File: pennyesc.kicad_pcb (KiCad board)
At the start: 4 copper layers, 60 x 19 mm, 48 parts, among them U1 STM32L011F4Ux, U2 MCT8316Z0RRGFR, U3 TMAG5273A1QDBVR

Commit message: finish v1 and order from jlcpcb
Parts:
- removed the C1 at (43.7, 50.1)
- removed the C2 at (44.3, 51.8)
- removed the C3 at (54.2, 55.4)
- removed the C4 at (52.0, 53.1)
- removed the C5 at (51.7, 56.0)
- removed the C6 at (52.2, 45.5)
- removed the C7 at (51.2, 43.8)
- removed the R1 at (52.4, 54.6)
- removed the R2 at (51.6, 47.1)
- removed the R3 at (55.9, 54.3)
- removed the R4 at (55.9, 55.2)
- removed the R5 at (45.0, 46.4)
- removed the R6 at (46.4, 45.0)
- removed the TP1 at (45.1, 47.4)
- removed the TP2 at (56.5, 50.5)
- removed the TP3 at (56.5, 49.4)
- removed the TP4 at (43.8, 51.2)
- removed the TP5 at (43.8, 49.2)
- removed the TP6 at (56.5, 45.5)
- removed the TP7 at (55.4, 44.1)
- removed the TP8 at (53.6, 44.0)
- removed the U1 at (46.5, 53.5)
- removed the U2 at (55.4, 50.0)
- removed the U3 at (47.2, 47.3)
- added TP10: TestPoint, pennyesc:Power_Pad_Rect, B.Cu at (56.1, 47.5)
- added TP11: TestPoint, pennyesc:TestPoint_Pad_1mm, B.Cu at (47.5, 53.7)
- added TP9: TestPoint, pennyesc:Power_Pad_Rect, B.Cu at (56.1, 52.5)
- TP1: footprint pennyesc:TestPoint_Pad_Rect -> pennyesc:TestPoint_Pad_1mm
- moved R1 21.7 mm to (52.6, 45.2), turned to 0 degrees
- moved R2 20.8 mm to (56.0, 45.0), turned to 90 degrees
- moved C5 20.5 mm to (51.6, 52.8)
- moved C4 20.5 mm to (51.6, 46.9), turned to -90 degrees
- moved R3 20.4 mm to (55.0, 45.0)
- moved C1 20.4 mm to (43.7, 50.1)
- moved R4 20.4 mm to (54.5, 43.6)
- moved TP8 20.4 mm to (56.3, 54.7)
- moved U1 20.4 mm to (46.5, 46.5)
- moved TP6 20.4 mm to (53.1, 55.9)
- moved R6 20.4 mm to (45.0, 53.6)
- moved U2 20.4 mm to (55.5, 50.0)
- moved U3 20.3 mm to (47.2, 52.8)
- moved R5 20.3 mm to (46.4, 55.0), turned to -45 degrees
- moved TP7 20.3 mm to (54.9, 55.8)
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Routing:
- net +3.3V: track 0.83 -> 24.9 mm, vias 2 -> 7
- net /UART_TX: track 0.00 -> 18.0 mm, vias 0 -> 1
- net /UART_RX: track 0.00 -> 16.2 mm, vias 0 -> 1
- net /SPI_MOSI: track 0.00 -> 14.4 mm, vias 0 -> 2
- net /SWCLK: track 0.00 -> 14.1 mm, vias 0 -> 1
- net /SWDIO: track 0.00 -> 13.1 mm, vias 0 -> 1
- net /SPI_MISO: track 0.00 -> 13.1 mm, vias 0 -> 2
- net /HALLB: track 0.00 -> 13.1 mm, vias 0 -> 2
- net /HALLA: track 1.10 -> 14.0 mm
- net GND: track 3.41 -> 14.9 mm, vias 0 -> 19
- net /HALLC: track 0.00 -> 11.0 mm, vias 0 -> 2
- net /SPI_SCLK: track 0.00 -> 10.6 mm, vias 0 -> 2
- net /I2C_SCL: track 0.00 -> 10.5 mm, vias 0 -> 2
- net /PWM: track 0.00 -> 10.0 mm, vias 0 -> 2
- net /SPI_CS: track 0.00 -> 9.75 mm, vias 0 -> 2
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- added copper zone on In1.Cu, net +3.3V
- added copper zone on F.Cu, net /OUTA
- added copper zone on F.Cu, net /OUTB
- added copper zone on F.Cu, net /OUTC
- added copper zone on B.Cu, net GND
- added copper zone on F.Cu, net GND
- added copper zone on In2.Cu, net GND
- added copper zone on B.Cu, net VBUS
- added copper zone on F.Cu, net VBUS
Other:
- board size 60 x 19 mm -> 15.9 x 14 mm
- board text added: "4.5-35"
- board text added: "GND"
- board text added: "RX"
- board text added: "TX"
- board text added: "V+"
- board text added: "gnd"
- board text added: "nrst"
- board text added: "pennyesc"
- board text added: "swclk"
- board text added: "swio"
- board text added: "v1"
- board text removed: "penny for scale"

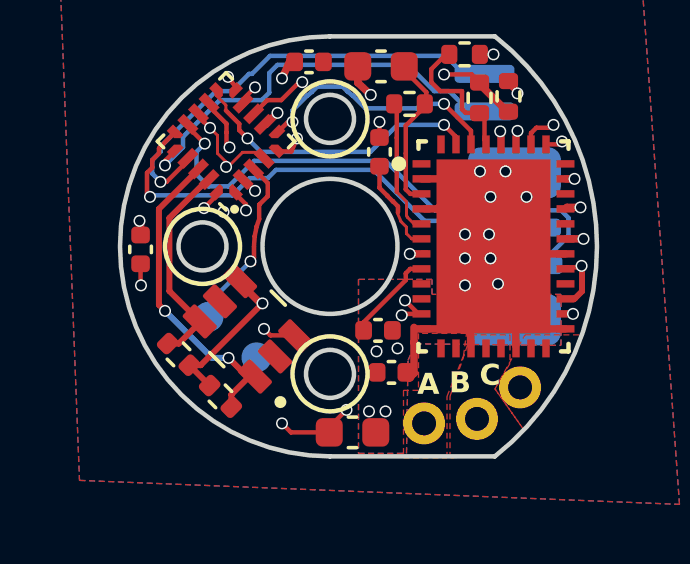
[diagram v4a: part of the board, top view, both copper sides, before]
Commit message: octant LUT for off axis magnetic encoder, staircase artifacts left
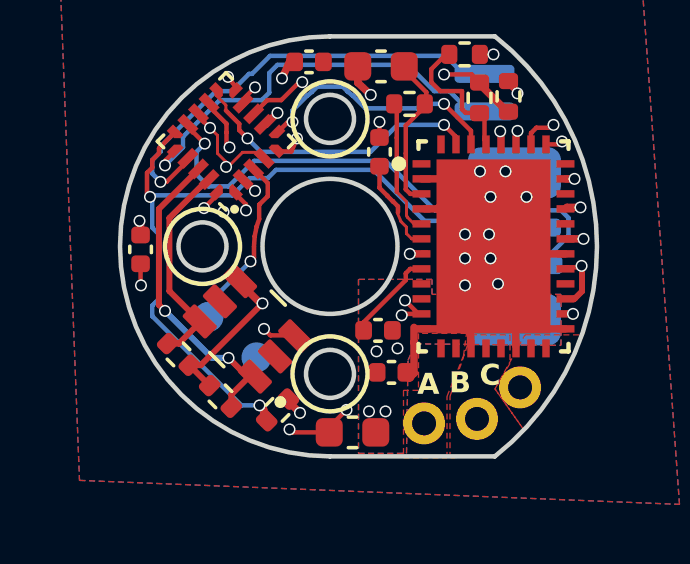
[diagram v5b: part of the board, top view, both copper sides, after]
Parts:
- added R8: 3.3k, Resistor_SMD:R_0402_1005Metric, F.Cu at (48.2, 55.5)
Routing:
- net /UART_RX: track 16.2 -> 25.9 mm, vias 1 -> 2
- net +3.3V: track 24.9 -> 25.5 mm, vias 7 -> 8
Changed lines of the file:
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@@
+  )
+  (footprint "Resistor_SMD:R_0402_1005Metric" (layer "F.Cu")
+    (at 48.25 55.45 -135)
+    (descr "Resistor SMD 0402 (1005 Metric), square (rectangular) end terminal, IPC_7351 nominal, (Body size source: IPC-SM-782 page 72, https://www.pcb-3d.com/wordpress/wp-content/uploads/ipc-sm-782a_amendment_1_and_2.pdf), generated with kicad-footprint-generator")
+    (tags "resistor")
+    (property "FT Rotation Offset" "")
+    (property "JLCPCB" "C25890")
+    (property "LCSC PN" "C25890")
+    (property "MP" "0402WGF3301TCE")
+    (property "Sheetfile" "pennyesc.kicad_sch")
+    (property "Sheetname" "")
+    (property "ki_description" "Resistor, small US symbol")
+    (property "ki_keywords" "r resistor")
+    (attr smd)
+    (fp_text reference "R8" (at 0 -1.17 45) (layer "F.SilkS") hide
+        (effects (font (size 1 1) (thickness 0.15)))
+    )
+    (fp_text value "3.3k" (at 0 1.17 45) (layer "F.Fab")
+        (effects (font (size 1 1) (thickness 0.15)))
+    )
+    (fp_text user "${REFERENCE}" (at 0 0 45) (layer "F.Fab")
+        (effects (font (size 0.26 0.26) (thickness 0.04)))
+    )
+    (fp_line (start -0.153641 -0.38) (end 0.153641 -0.38)
+      (stroke (width 0.12) (type solid)) (layer "F.SilkS"))
+    (fp_line (start -0.153641 0.38) (end 0.153641 0.38)
+      (stroke (width 0.12) (type solid)) (layer "F.SilkS"))
+    (fp_line (start -0.93 -0.47) (end 0.93 -0.47)
+      (stroke (width 0.05) (type solid)) (layer "F.CrtYd"))
+    (fp_line (start -0.93 0.47) (end -0.93 -0.47)
+      (stroke (width 0.05) (type solid)) (layer "F.CrtYd"))
+    (fp_line (start 0.93 -0.47) (end 0.93 0.47)
+      (stroke (width 0.05) (type solid)) (layer "F.CrtYd"))
+    (fp_line (start 0.93 0.47) (end -0.93 0.47)
+      (stroke (width 0.05) (type solid)) (layer "F.CrtYd"))
+    (fp_line (start -0.525 -0.27) (end 0.525 -0.27)
+      (stroke (width 0.1) (type solid)) (layer "F.Fab"))
+    (fp_line (start -0.525 0.27) (end -0.525 -0.27)
+      (stroke (width 0.1) (type solid)) (layer "F.Fab"))
+    (fp_line (start 0.525 -0.27) (end 0.525 0.27)
+      (stroke (width 0.1) (type solid)) (layer "F.Fab"))
+    (fp_line (start 0.525 0.27) (end -0.525 0.27)
+      (stroke (width 0.1) (type solid)) (layer "F.Fab"))
+    (pad "1" smd roundrect (at -0.51 0 225) (size 0.54 0.64) (layers "F.Cu" "F.Paste" "F.Mask") (roundrect_rratio 0.25)
+      (net 2 "+3.3V") (pintype "passive"))
+    (pad "2" smd roundrect (at 0.51 0 225) (size 0.54 0.64) (layers "F.Cu" "F.Paste" "F.Mask") (roundrect_rratio 0.25)
+      (net 9 "/UART_RX") (pintype "passive"))
+    (model "${KICAD6_3DMODEL_DIR}/Resistor_SMD.3dshapes/R_0402_1005Metric.wrl"
+      (offset (xyz 0 0 0))
+      (scale (xyz 1 1 1))
+      (rotate (xyz 0 0 0))
+    )
   )
   (footprint "Resistor_SMD:R_0402_1005Metric" (layer "F.Cu")
@@
   (segment (start 49.975 56.025) (end 50.55 55.45) (width 0.15) (layer "F.Cu") (net 1))
   (segment (start 53.572764 48.75) (end 53.722675 48.600089) (width 0.25) (layer "F.Cu") (net 1))
+  (segment (start 48.65 56.1) (end 48.75 56.2) (width 0.15) (layer "F.Cu") (net 1))
   (segment (start 46.55 46.6) (end 46.65 46.7) (width 0.15) (layer "F.Cu") (net 1))
   (segment (start 48.80917 52.965668) (end 48.015668 52.965668) (width 0.15) (layer "F.Cu") (net 1))
   (segment (start 52.8 53.2) (end 52.8 52.7) (width 0.25) (layer "F.Cu") (net 1))
   (segment (start 46.55 45.913172) (end 46.55 46.2) (width 0.15) (layer "F.Cu") (net 1))
+  (segment (start 48.75 56.2) (end 49.975 56.2) (width 0.15) (layer "F.Cu") (net 1))
   (segment (start 53.15 48.75) (end 53.572764 48.75) (width 0.25) (layer "F.Cu") (net 1))
   (segment (start 56.185876 53.300089) (end 56.185876 52.61329) (width 0.25) (layer "F.Cu") (net 1))
@@
   (segment (start 53.05 52.75) (end 53.75 52.75) (width 0.25) (layer "F.Cu") (net 1))
   (segment (start 46.55 46.2) (end 46.55 46.6) (width 0.15) (layer "F.Cu") (net 1))
-  (segment (start 49.975 56.2) (end 48.7 56.2) (width 0.15) (layer "F.Cu") (net 1))
   (segment (start 55.499589 43.600089) (end 54.995876 43.600089) (width 0.15) (layer "F.Cu") (net 1))
-  (segment (start 48.7 56.2) (end 48.4 55.9) (width 0.15) (layer "F.Cu") (net 1))
   (segment (start 54.685876 53.300089) (end 54.685876 52.636888) (width 0.25) (layer "F.Cu") (net 1))
   (via (at 54.5 51.3) (size 0.4) (drill 0.3) (layers "F.Cu" "B.Cu") (net 1))
@@
   (via (at 55.85 47.5) (size 0.4) (drill 0.3) (layers "F.Cu" "B.Cu") (net 1))
   (via (at 55 47.5) (size 0.4) (drill 0.3) (layers "F.Cu" "B.Cu") (net 1))
-  (via (at 48.4 55.9) (size 0.4) (drill 0.3) (layers "F.Cu" "B.Cu") (net 1))
+  (via (at 48.65 56.1) (size 0.4) (drill 0.3) (layers "F.Cu" "B.Cu") (net 1))
   (via (at 51.357816 44.95) (size 0.4) (drill 0.3) (layers "F.Cu" "B.Cu") (net 1))
   (via (at 54.5 49.6) (size 0.4) (drill 0.3) (layers "F.Cu" "B.Cu") (net 1))
@@
   (segment (start 43.685876 51.185376) (end 43.685876 50.580089) (width 0.15) (layer "F.Cu") (net 2))
   (segment (start 46.535876 47.185876) (end 46.25 46.9) (width 0.1) (layer "F.Cu") (net 2))
+  (segment (start 48.639376 55.189376) (end 49 55.55) (width 0.25) (layer "F.Cu") (net 2))
   (segment (start 45.616637 45.58085) (end 45.616637 45.666637) (width 0.15) (layer "F.Cu") (net 2))
   (segment (start 48.4 44.4) (end 48.65 43.85) (width 0.25) (layer "F.Cu") (net 2))
@@
   (segment (start 57.885876 50.700089) (end 58.335876 50.700089) (width 0.15) (layer "F.Cu") (net 2))
   (segment (start 54.719589 44.269589) (end 54.95 44.5) (width 0.15) (layer "F.Cu") (net 2))
+  (segment (start 48.510624 55.189376) (end 48.639376 55.189376) (width 0.25) (layer "F.Cu") (net 2))
   (segment (start 45.310624 53.960624) (end 45.95 54.6) (width 0.2) (layer "F.Cu") (net 2))
   (segment (start 46.25 46.3) (end 46 46.05) (width 0.1) (layer "F.Cu") (net 2))
@@
   (via (at 43.7 51.3) (size 0.4) (drill 0.3) (layers "F.Cu" "B.Cu") (net 2))
   (via (at 48.4 44.4) (size 0.4) (drill 0.3) (layers "F.Cu" "B.Cu") (net 2))
+  (via (at 49 55.55) (size 0.4) (drill 0.3) (layers "F.Cu" "B.Cu") (net 2))
   (via (at 46 46.05) (size 0.4) (drill 0.3) (layers "F.Cu" "B.Cu") (net 2))
   (via (at 47.75 51.9) (size 0.4) (drill 0.3) (layers "F.Cu" "B.Cu") (net 2))
@@
   (segment (start 44.3 46.898959) (end 44.075 47.123959) (width 0.15) (layer "F.Cu") (net 9))
   (segment (start 44.075 47.375) (end 43.9 47.55) (width 0.15) (layer "F.Cu") (net 9))
+  (segment (start 47.789376 55.439376) (end 47.65 55.3) (width 0.25) (layer "F.Cu") (net 9))
   (segment (start 43.9 47.55) (end 43.9 48.25) (width 0.15) (layer "F.Cu") (net 9))
   (segment (start 44.075 47.123959) (end 44.075 47.375) (width 0.15) (layer "F.Cu") (net 9))
+  (segment (start 47.789376 55.910624) (end 47.789376 55.439376) (width 0.25) (layer "F.Cu") (net 9))
   (segment (start 44.785787 46.164213) (end 44.785787 46.244788) (width 0.15) (layer "F.Cu") (net 9))
+  (via (at 47.65 55.3) (size 0.4) (drill 0.3) (layers "F.Cu" "B.Cu") (net 9))
   (via (at 44 48.35) (size 0.4) (drill 0.3) (layers "F.Cu" "B.Cu") (net 9))
+  (segment (start 47.048959 55.3) (end 47.65 55.3) (width 0.15) (layer "B.Cu") (net 9))
   (segment (start 51.45 47.45) (end 48.199569 47.45) (width 0.15) (layer "B.Cu") (net 9))
+  (segment (start 44.323959 51.725) (end 44.075 51.973959) (width 0.15) (layer "B.Cu") (net 9))
+  (segment (start 44.075 48.425) (end 44.075 49.375) (width 0.15) (layer "B.Cu") (net 9))
+  (segment (start 44.075 52.326041) (end 47.048959 55.3) (width 0.15) (layer "B.Cu") (net 9))
   (segment (start 44.05 48.3) (end 44 48.35) (width 0.15) (layer "B.Cu") (net 9))
   (segment (start 47.323959 47.725) (end 46.748959 48.3) (width 0.15) (layer "B.Cu") (net 9))
   (segment (start 47.924569 47.725) (end 47.323959 47.725) (width 0.15) (layer "B.Cu") (net 9))
   (segment (start 46.748959 48.3) (end 44.05 48.3) (width 0.15) (layer "B.Cu") (net 9))
+  (segment (start 44 48.35) (end 44.075 48.425) (width 0.15) (layer "B.Cu") (net 9))
+  (segment (start 44.323959 49.623959) (end 44.323959 51.725) (width 0.15) (layer "B.Cu") (net 9))
   (segment (start 56.485876 49.350089) (end 56.149911 49.350089) (width 0.15) (layer "B.Cu") (net 9))
   (segment (start 56.149911 49.350089) (end 55.949822 49.15) (width 0.15) (layer "B.Cu") (net 9))
   (segment (start 48.199569 47.45) (end 47.924569 47.725) (width 0.15) (layer "B.Cu") (net 9))
+  (segment (start 44.075 51.973959) (end 44.075 52.326041) (width 0.15) (layer "B.Cu") (net 9))
   (segment (start 55.949822 49.15) (end 53.15 49.15) (width 0.15) (layer "B.Cu") (net 9))
+  (segment (start 44.075 49.375) (end 44.323959 49.623959) (width 0.15) (layer "B.Cu") (net 9))
   (segment (start 53.15 49.15) (end 51.45 47.45) (width 0.15) (layer "B.Cu") (net 9))
   (segment (start 44.5 47.15) (end 44.85 46.8) (width 0.15) (layer "F.Cu") (net 10))

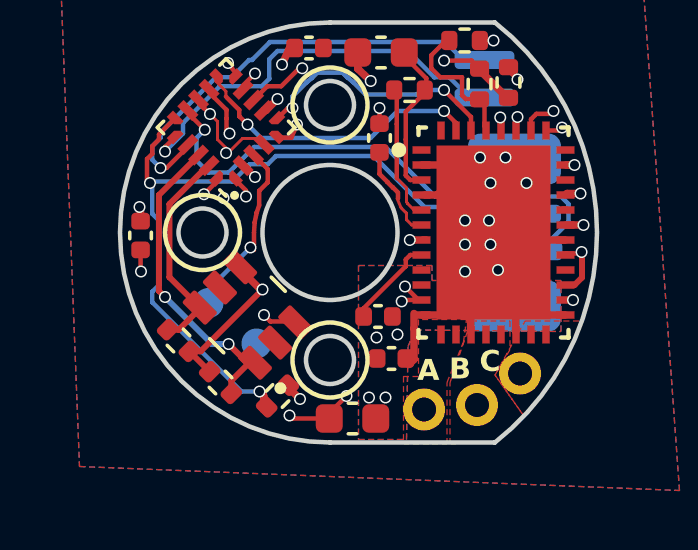
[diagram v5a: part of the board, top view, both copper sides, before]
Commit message: pennyesc pcb v2 ordered
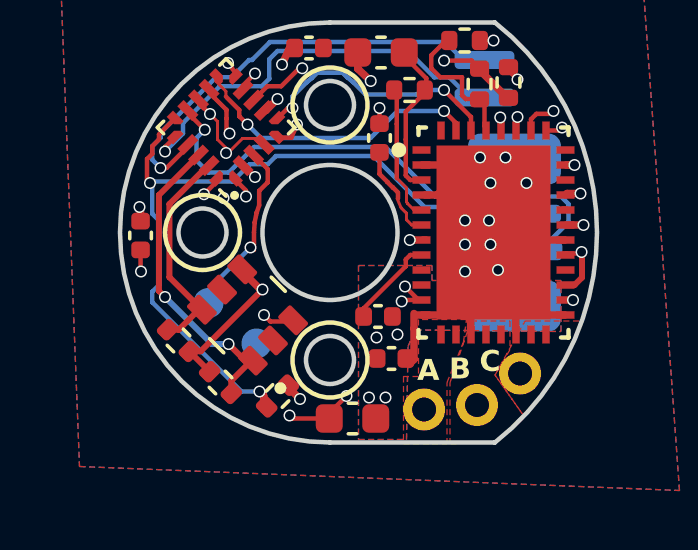
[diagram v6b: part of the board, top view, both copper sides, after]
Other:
- board text added: "v2"
- board text removed: "v1"
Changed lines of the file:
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@@
   (title_block
     (title "PennyESC")
-    (date "2025-10-22")
-    (rev "1")
+    (date "2025-12-25")
+    (rev "2")
     (company "Christopher Xu")
   )
@@
     (fp_circle (center -2.5 -0.95) (end -2.4 -0.95)
       (stroke (width 0.2) (type solid)) (fill none) (layer "F.Fab"))
-    (pad "1" smd roundrect (at -1.3 -0.95 135) (size 1.1 0.6) (layers "F.Cu" "F.Paste" "F.Mask") (roundrect_rratio 0.125)
+    (pad "1" smd roundrect (at -1.2 -0.95 135) (size 0.9 0.6) (layers "F.Cu" "F.Paste" "F.Mask") (roundrect_rratio 0.125)
       (net 20 "/I2C_SCL") (pinfunction "SCL") (pintype "bidirectional"))
-    (pad "2" smd roundrect (at -1.3 0 135) (size 1.1 0.6) (layers "F.Cu" "F.Paste" "F.Mask") (roundrect_rratio 0.125)
+    (pad "2" smd roundrect (at -1.2 0 135) (size 0.9 0.6) (layers "F.Cu" "F.Paste" "F.Mask") (roundrect_rratio 0.125)
       (net 1 "GND") (pinfunction "GND") (pintype "power_in"))
-    (pad "3" smd roundrect (at -1.3 0.95 135) (size 1.1 0.6) (layers "F.Cu" "F.Paste" "F.Mask") (roundrect_rratio 0.125)
+    (pad "3" smd roundrect (at -1.2 0.95 135) (size 0.9 0.6) (layers "F.Cu" "F.Paste" "F.Mask") (roundrect_rratio 0.125)
       (net 1 "GND") (pinfunction "TEST") (pintype "input"))
-    (pad "4" smd roundrect (at 1.3 0.95 135) (size 1.1 0.6) (layers "F.Cu" "F.Paste" "F.Mask") (roundrect_rratio 0.125)
+    (pad "4" smd roundrect (at 1.2 0.95 135) (size 0.9 0.6) (layers "F.Cu" "F.Paste" "F.Mask") (roundrect_rratio 0.125)
       (net 2 "+3.3V") (pinfunction "VCC") (pintype "power_in"))
-    (pad "5" smd roundrect (at 1.3 0 135) (size 1.1 0.6) (layers "F.Cu" "F.Paste" "F.Mask") (roundrect_rratio 0.125)
+    (pad "5" smd roundrect (at 1.2 0 135) (size 0.9 0.6) (layers "F.Cu" "F.Paste" "F.Mask") (roundrect_rratio 0.125)
       (net 36 "unconnected-(U3-~{INT}-Pad5)") (pinfunction "~{INT}") (pintype "bidirectional+no_connect"))
-    (pad "6" smd roundrect (at 1.3 -0.95 135) (size 1.1 0.6) (layers "F.Cu" "F.Paste" "F.Mask") (roundrect_rratio 0.125)
+    (pad "6" smd roundrect (at 1.2 -0.95 135) (size 0.9 0.6) (layers "F.Cu" "F.Paste" "F.Mask") (roundrect_rratio 0.125)
       (net 21 "/I2C_SDA") (pinfunction "SDA") (pintype "bidirectional"))
     (model "${KIPRJMOD}/pennyesc.pretty/TMAG5273A1QDBVR.step"
@@
     (effects (font (size 0.7 0.7) (thickness 0.15)) (justify left bottom mirror))
   )
-  (gr_text "v1" (at 48.35 46.85 45) (layer "B.SilkS")
+  (gr_text "v2" (at 48.35 46.85 45) (layer "B.SilkS")
     (effects (font (size 1 1) (thickness 0.15)) (justify left bottom mirror))
   )
